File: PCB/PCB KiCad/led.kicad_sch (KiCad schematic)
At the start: 22 parts, among them U5 TLC59208FIPWR

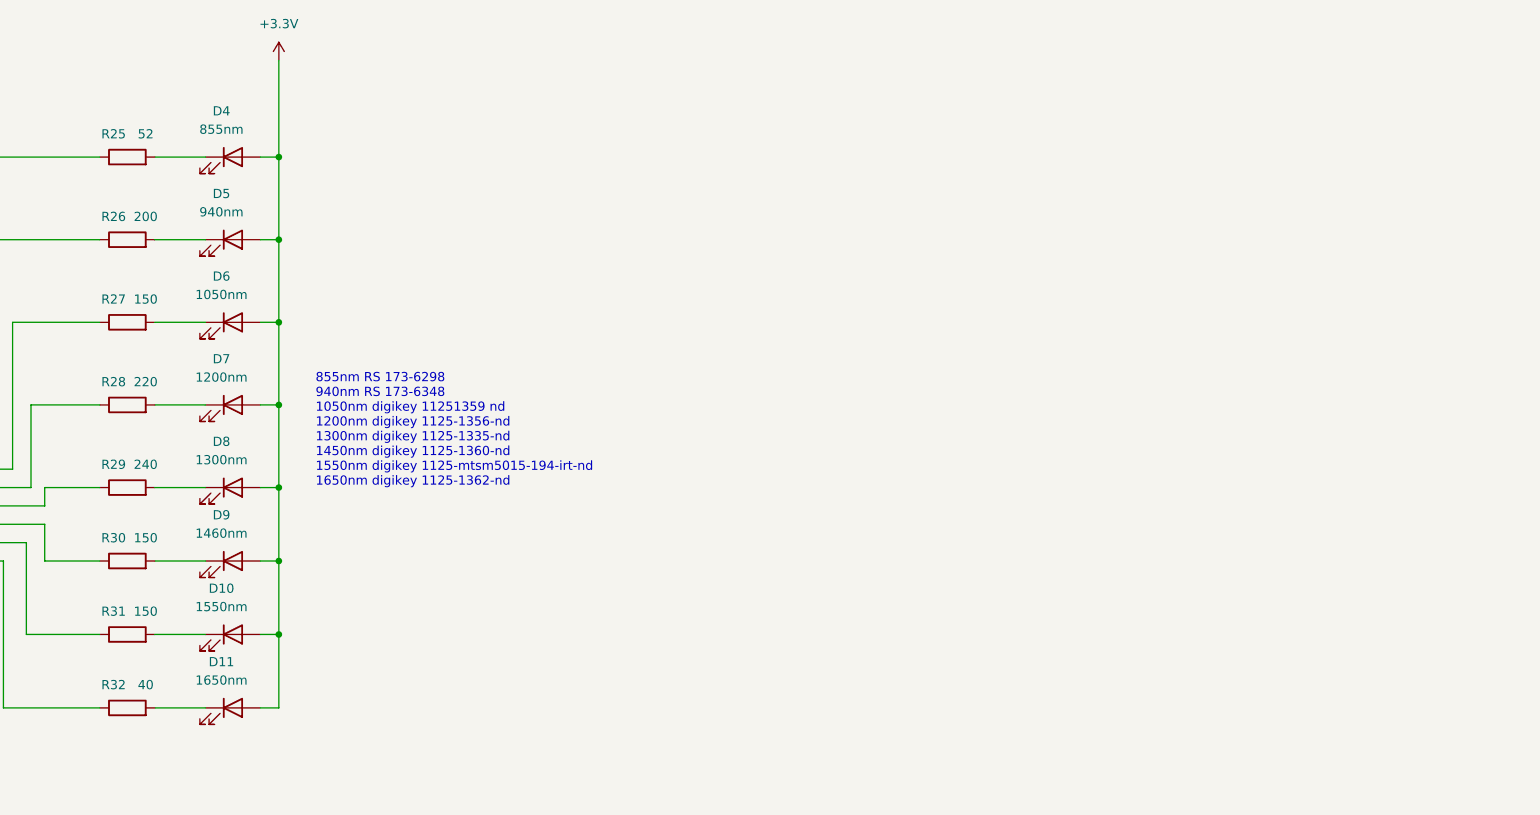
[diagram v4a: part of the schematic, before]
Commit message: adds correct values of current limiting resistors for LEDs
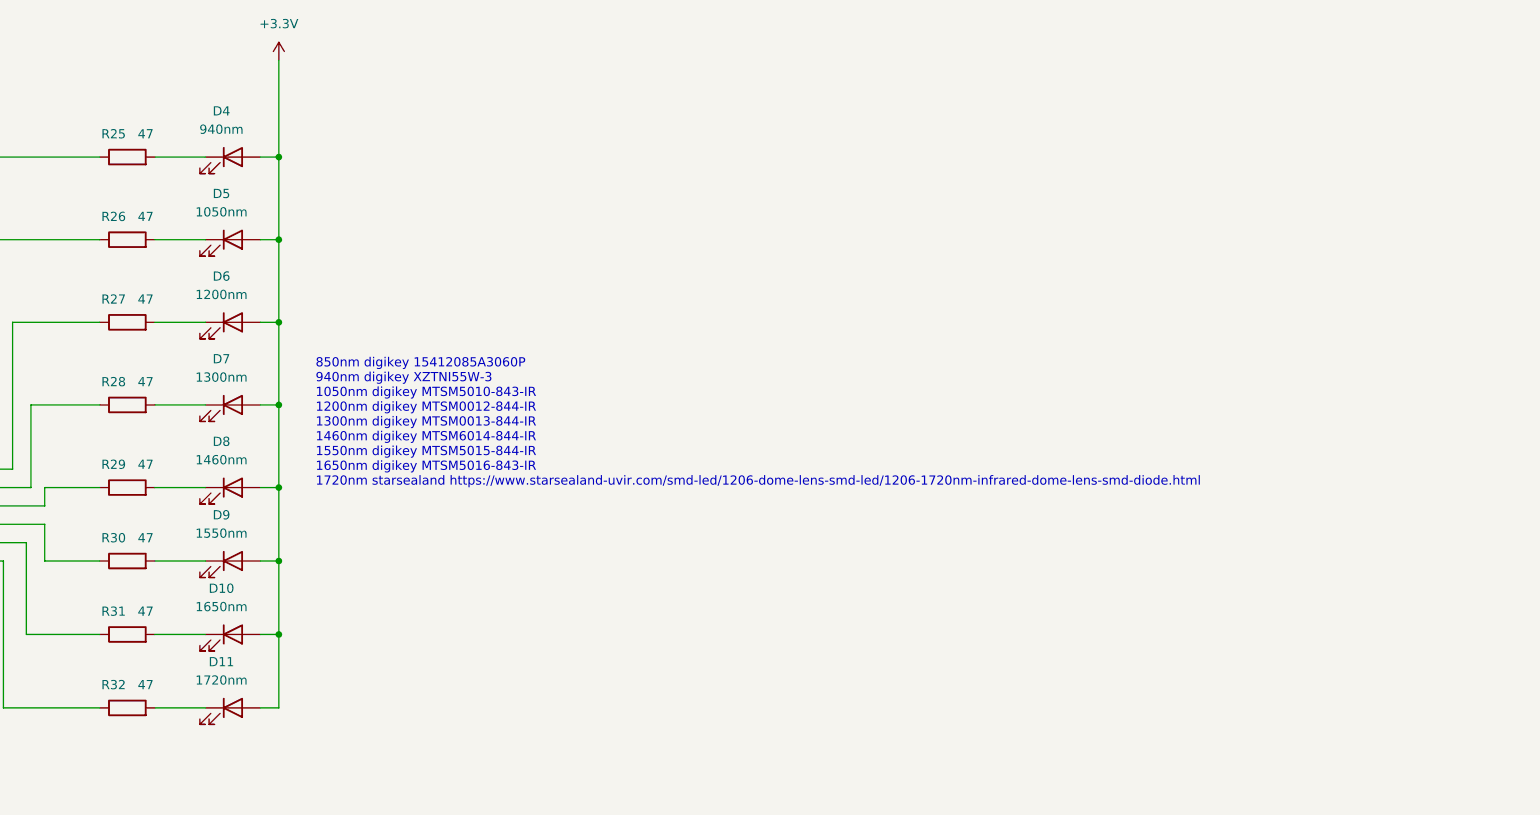
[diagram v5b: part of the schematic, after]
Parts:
- D10: value 1550nm -> 1650nm
- D11: value 1650nm -> 1720nm
- D4: value 855nm -> 940nm
- D5: value 940nm -> 1050nm
- D6: value 1050nm -> 1200nm
- D7: value 1200nm -> 1300nm
- D8: value 1300nm -> 1460nm
- D9: value 1460nm -> 1550nm
- R25: value 52 -> 47
- R26: value 200 -> 47
- R27, R30, R31: value 150 -> 47
- R28: value 220 -> 47
- R29: value 240 -> 47
- R32: value 40 -> 47
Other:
- note added: "850nm digikey 15412085A3060P 940nm digikey XZTNI55W-3 1050nm digikey MTSM5010-843-IR 1200nm digikey MTSM0012-844-IR 1300nm digikey MTSM0013-844-IR 1460nm digikey MTSM6014-844-IR 1550nm digikey MTSM5015-844-IR 1650nm digikey MTSM5016-843-IR 1720nm starsealand https://www.starsealand-uvir.com/smd-led/1206-dome-lens-smd-led/1206-1720nm-infrared-dome-lens-smd-diode.html"
- note removed: "855nm RS 173-6298 940nm RS 173-6348 1050nm digikey 11251359 nd 1200nm digikey 1125-1356-nd 1300nm digikey 1125-1335-nd 1450nm digikey 1125-1360-nd 1550nm digikey 1125-mtsm5015-194-irt-nd 1650nm digikey 1125-1362-nd"
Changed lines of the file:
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@@
     (stroke (width 0) (type default) (color 0 0 0 0))
   )
-  (text "855nm RS 173-6298\n940nm RS 173-6348\n1050nm digikey 11251359 nd\n1200nm digikey 1125-1356-nd\n1300nm digikey 1125-1335-nd\n1450nm digikey 1125-1360-nd\n1550nm digikey 1125-mtsm5015-194-irt-nd\n1650nm digikey 1125-1362-nd"
+  (text "850nm digikey 15412085A3060P\n940nm digikey XZTNI55W-3\n1050nm digikey MTSM5010-843-IR\n1200nm digikey MTSM0012-844-IR\n1300nm digikey MTSM0013-844-IR\n1460nm digikey MTSM6014-844-IR\n1550nm digikey MTSM5015-844-IR\n1650nm digikey MTSM5016-843-IR\n1720nm starsealand https://www.starsealand-uvir.com/smd-led/1206-dome-lens-smd-led/1206-1720nm-infrared-dome-lens-smd-diode.html\n"
     (at 213.36 100.33 0)
     (effects (font (size 1.27 1.27)) (justify left bottom))
@@
     (in_bom yes) (on_board yes) (fields_autoplaced)
     (property "Reference" "D8" (id 0) (at 200.3425 93.98 0))
-    (property "Value" "1300nm" (id 1) (at 200.3425 96.52 0))
+    (property "Value" "1460nm" (id 1) (at 200.3425 96.52 0))
     (property "Footprint" "LED_SMD:LED_1206_3216Metric_Pad1.42x1.75mm_HandSolder" (id 2) (at 201.93 100.33 0)
       (effects (font (size 1.27 1.27)) hide)
@@
     (in_bom yes) (on_board yes)
     (property "Reference" "R32" (id 0) (at 185.42 127.635 90))
-    (property "Value" "40" (id 1) (at 189.865 127.635 90))
+    (property "Value" "47" (id 1) (at 189.865 127.635 90))
     (property "Footprint" "Resistor_SMD:R_0805_2012Metric_Pad1.20x1.40mm_HandSolder" (id 2) (at 187.325 132.588 90)
       (effects (font (size 1.27 1.27)) hide)
@@
     (in_bom yes) (on_board yes)
     (property "Reference" "R26" (id 0) (at 185.42 62.865 90))
-    (property "Value" "200" (id 1) (at 189.865 62.865 90))
+    (property "Value" "47" (id 1) (at 189.865 62.865 90))
     (property "Footprint" "Resistor_SMD:R_0805_2012Metric_Pad1.20x1.40mm_HandSolder" (id 2) (at 187.325 67.818 90)
       (effects (font (size 1.27 1.27)) hide)
@@
     (in_bom yes) (on_board yes) (fields_autoplaced)
     (property "Reference" "D9" (id 0) (at 200.3425 104.14 0))
-    (property "Value" "1460nm" (id 1) (at 200.3425 106.68 0))
+    (property "Value" "1550nm" (id 1) (at 200.3425 106.68 0))
     (property "Footprint" "LED_SMD:LED_1206_3216Metric_Pad1.42x1.75mm_HandSolder" (id 2) (at 201.93 110.49 0)
       (effects (font (size 1.27 1.27)) hide)
@@
     (in_bom yes) (on_board yes) (fields_autoplaced)
     (property "Reference" "D4" (id 0) (at 200.3425 48.26 0))
-    (property "Value" "855nm" (id 1) (at 200.3425 50.8 0))
+    (property "Value" "940nm" (id 1) (at 200.3425 50.8 0))
     (property "Footprint" "LED_SMD:LED_1206_3216Metric_Pad1.42x1.75mm_HandSolder" (id 2) (at 201.93 54.61 0)
       (effects (font (size 1.27 1.27)) hide)
@@
     (in_bom yes) (on_board yes) (fields_autoplaced)
     (property "Reference" "D7" (id 0) (at 200.3425 82.55 0))
-    (property "Value" "1200nm" (id 1) (at 200.3425 85.09 0))
+    (property "Value" "1300nm" (id 1) (at 200.3425 85.09 0))
     (property "Footprint" "LED_SMD:LED_1206_3216Metric_Pad1.42x1.75mm_HandSolder" (id 2) (at 201.93 88.9 0)
       (effects (font (size 1.27 1.27)) hide)
@@
     (in_bom yes) (on_board yes)
     (property "Reference" "R25" (id 0) (at 185.42 51.435 90))
-    (property "Value" "52" (id 1) (at 189.865 51.435 90))
+    (property "Value" "47" (id 1) (at 189.865 51.435 90))
     (property "Footprint" "Resistor_SMD:R_0805_2012Metric_Pad1.20x1.40mm_HandSolder" (id 2) (at 187.325 56.388 90)
       (effects (font (size 1.27 1.27)) hide)
@@
     (in_bom yes) (on_board yes)
     (property "Reference" "R30" (id 0) (at 185.42 107.315 90))
-    (property "Value" "150" (id 1) (at 189.865 107.315 90))
+    (property "Value" "47" (id 1) (at 189.865 107.315 90))
     (property "Footprint" "Resistor_SMD:R_0805_2012Metric_Pad1.20x1.40mm_HandSolder" (id 2) (at 187.325 112.268 90)
       (effects (font (size 1.27 1.27)) hide)
@@
     (in_bom yes) (on_board yes) (fields_autoplaced)
     (property "Reference" "D11" (id 0) (at 200.3425 124.46 0))
-    (property "Value" "1650nm" (id 1) (at 200.3425 127 0))
+    (property "Value" "1720nm" (id 1) (at 200.3425 127 0))
     (property "Footprint" "LED_SMD:LED_1206_3216Metric_Pad1.42x1.75mm_HandSolder" (id 2) (at 201.93 130.81 0)
       (effects (font (size 1.27 1.27)) hide)
@@
     (in_bom yes) (on_board yes)
     (property "Reference" "R29" (id 0) (at 185.42 97.155 90))
-    (property "Value" "240" (id 1) (at 189.865 97.155 90))
+    (property "Value" "47" (id 1) (at 189.865 97.155 90))
     (property "Footprint" "Resistor_SMD:R_0805_2012Metric_Pad1.20x1.40mm_HandSolder" (id 2) (at 187.325 102.108 90)
       (effects (font (size 1.27 1.27)) hide)
@@
     (in_bom yes) (on_board yes) (fields_autoplaced)
     (property "Reference" "D6" (id 0) (at 200.3425 71.12 0))
-    (property "Value" "1050nm" (id 1) (at 200.3425 73.66 0))
+    (property "Value" "1200nm" (id 1) (at 200.3425 73.66 0))
     (property "Footprint" "LED_SMD:LED_1206_3216Metric_Pad1.42x1.75mm_HandSolder" (id 2) (at 201.93 77.47 0)
       (effects (font (size 1.27 1.27)) hide)
@@
     (in_bom yes) (on_board yes) (fields_autoplaced)
     (property "Reference" "D5" (id 0) (at 200.3425 59.69 0))
-    (property "Value" "940nm" (id 1) (at 200.3425 62.23 0))
+    (property "Value" "1050nm" (id 1) (at 200.3425 62.23 0))
     (property "Footprint" "LED_SMD:LED_1206_3216Metric_Pad1.42x1.75mm_HandSolder" (id 2) (at 201.93 66.04 0)
       (effects (font (size 1.27 1.27)) hide)
@@
     (in_bom yes) (on_board yes)
     (property "Reference" "R31" (id 0) (at 185.42 117.475 90))
-    (property "Value" "150" (id 1) (at 189.865 117.475 90))
+    (property "Value" "47" (id 1) (at 189.865 117.475 90))
     (property "Footprint" "Resistor_SMD:R_0805_2012Metric_Pad1.20x1.40mm_HandSolder" (id 2) (at 187.325 122.428 90)
       (effects (font (size 1.27 1.27)) hide)
@@
     (in_bom yes) (on_board yes)
     (property "Reference" "R27" (id 0) (at 185.42 74.295 90))
-    (property "Value" "150" (id 1) (at 189.865 74.295 90))
+    (property "Value" "47" (id 1) (at 189.865 74.295 90))
     (property "Footprint" "Resistor_SMD:R_0805_2012Metric_Pad1.20x1.40mm_HandSolder" (id 2) (at 187.325 79.248 90)
       (effects (font (size 1.27 1.27)) hide)
@@
     (in_bom yes) (on_board yes)
     (property "Reference" "R28" (id 0) (at 185.42 85.725 90))
-    (property "Value" "220" (id 1) (at 189.865 85.725 90))
+    (property "Value" "47" (id 1) (at 189.865 85.725 90))
     (property "Footprint" "Resistor_SMD:R_0805_2012Metric_Pad1.20x1.40mm_HandSolder" (id 2) (at 187.325 90.678 90)
       (effects (font (size 1.27 1.27)) hide)
@@
     (in_bom yes) (on_board yes) (fields_autoplaced)
     (property "Reference" "D10" (id 0) (at 200.3425 114.3 0))
-    (property "Value" "1550nm" (id 1) (at 200.3425 116.84 0))
+    (property "Value" "1650nm" (id 1) (at 200.3425 116.84 0))
     (property "Footprint" "LED_SMD:LED_1206_3216Metric_Pad1.42x1.75mm_HandSolder" (id 2) (at 201.93 120.65 0)
       (effects (font (size 1.27 1.27)) hide)

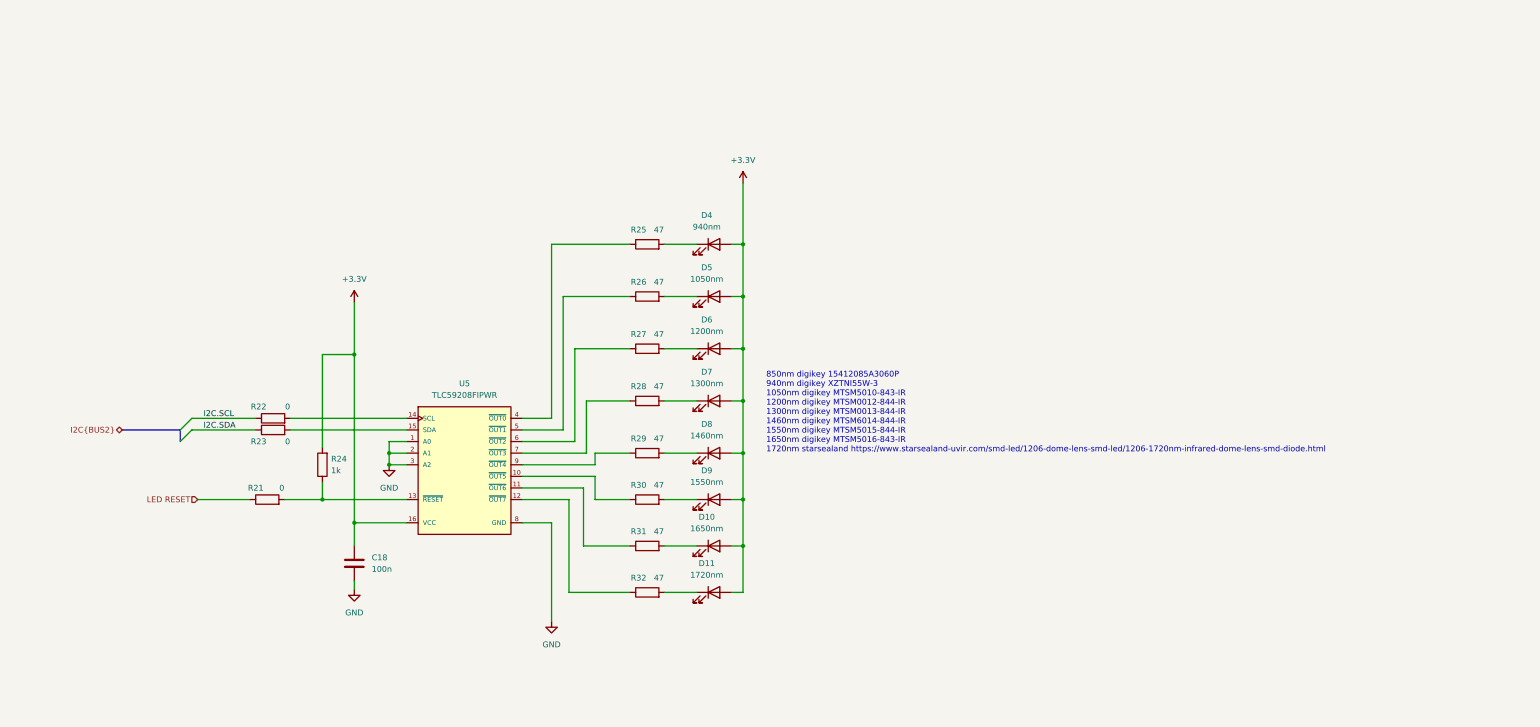
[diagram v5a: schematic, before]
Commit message: v2.2.0 first attempt for new ICs
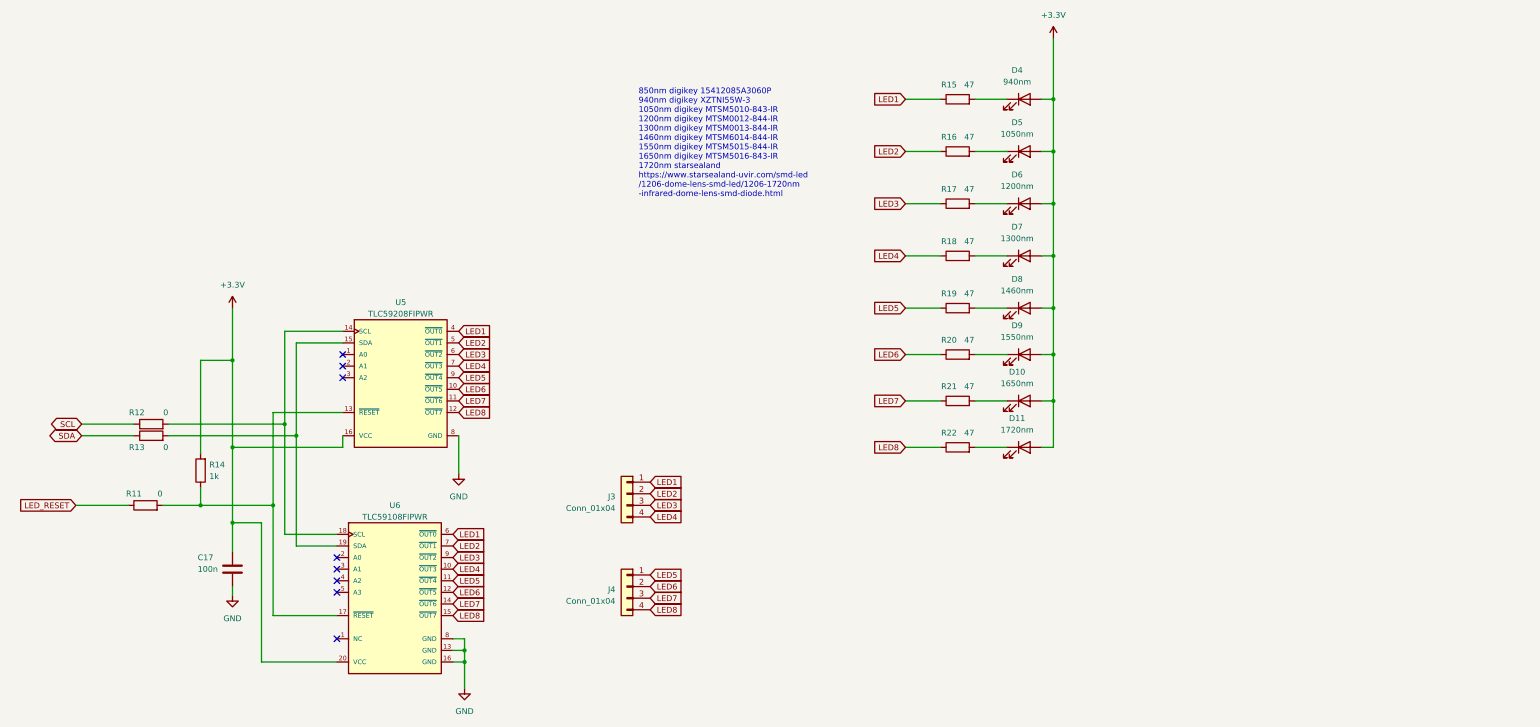
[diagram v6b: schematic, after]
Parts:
- added J3, J4: Conn_01x04, Connector_PinSocket_2.54mm:PinSocket_1x04_P2.54mm_Vertical, symbol Connector_Generic:Conn_01x04
- added U6: TLC59108FIPWR, TLC59108:Texas_Instruments-TLC59108FIPWR-Level_A, symbol TLC59108:TLC59108FIPWR
- renumbered C18 to C17, R21 to R11, R22 to R12, R23 to R13, R24 to R14, R25 to R15, R26 to R16, R27 to R17, R28 to R18, R29 to R19, R30 to R20, R31 to R21, R32 to R22
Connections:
- net +3V3: now also U6.20 (VCC)
- net GND: now also U6.13 (GND), U6.16 (GND), U6.8 (GND); no longer U5.1 (A0), U5.2 (A1), U5.3 (A2)
- net at R13.2, U5.15 (SDA): now also U6.19 (SDA)
- net LED8: now reaches R22.1, U5.12 (~{OUT7})
- net LED8: now also J4.4 (Pin_4), U6.15 (~{OUT7})
- net LED6: now reaches R20.1, U5.10 (~{OUT5})
- net LED6: now also J4.2 (Pin_2), U6.12 (~{OUT5})
- net LED7: now reaches R21.1, U5.11 (~{OUT6})
- net LED7: now also J4.3 (Pin_3), U6.14 (~{OUT6})
- net at R11.2, R14.1, U5.13 (~{RESET}): now also U6.17 (~{RESET})
- net at R12.2, U5.14 (SCL): now also U6.18 (SCL)
- net LED1: now reaches R15.1, U5.4 (~{OUT0})
- net LED1: now also J3.1 (Pin_1), U6.6 (~{OUT0})
- net LED2: now reaches R16.1, U5.5 (~{OUT1})
- net LED2: now also J3.2 (Pin_2), U6.7 (~{OUT1})
- net LED3: now reaches R17.1, U5.6 (~{OUT2})
- net LED3: now also J3.3 (Pin_3), U6.9 (~{OUT2})
- net LED4: now reaches R18.1, U5.7 (~{OUT3})
- net LED4: now also J3.4 (Pin_4), U6.10 (~{OUT3})
- net LED5: now reaches R19.1, U5.9 (~{OUT4})
- net LED5: now also J4.1 (Pin_1), U6.11 (~{OUT4})
- net I2C.SCL renamed SCL
- net I2C.SDA renamed SDA
- net LED RESET renamed LED_RESET
- no-connect marks 0 -> 8
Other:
- note added: "850nm digikey 15412085A3060P 940nm digikey XZTNI55W-3 1050nm digikey MTSM5010-843-IR 1200nm digikey MTSM0012-844-IR 1300nm digikey MTSM0013-844-IR 1460nm digikey MTSM6014-844-IR 1550nm digikey MTSM5015-844-IR 1650nm digikey MTSM5016-843-IR 1720nm starsealand https://www.starsealand-uvir.com/smd-led /1206-dome-lens-smd-led/1206-1720nm -infrared-dome-lens-smd-diode.html"
- note removed: "850nm digikey 15412085A3060P 940nm digikey XZTNI55W-3 1050nm digikey MTSM5010-843-IR 1200nm digikey MTSM0012-844-IR 1300nm digikey MTSM0013-844-IR 1460nm digikey MTSM6014-844-IR 1550nm digikey MTSM5015-844-IR 1650nm digikey MTSM5016-843-IR 1720nm starsealand https://www.starsealand-uvir.com/smd-led/1206-dome-lens-smd-led/1206-1720nm-infrared-dome-lens-smd-diode.html"
- moved on the sheet: C17, D10, D11, D4, D5, D6, D7, D8, D9, R11, R12, R13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
